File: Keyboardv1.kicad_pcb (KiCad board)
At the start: 2 copper layers, 168 parts, among them SW1 SW_Push_45deg, SW10 SW_Push_45deg, SW11 SW_Push_45deg, SW12 SW_Push_45deg, SW13 SW_Push_45deg, SW14 SW_Push_45deg, SW15 SW_Push_45deg, SW16 SW_Push_45deg, SW17 SW_Push_45deg, SW18 SW_Push_45deg, SW19 SW_Push_45deg, SW2 SW_Push_45deg, SW20 SW_Push_45deg, SW21 SW_Push_45deg, SW22 SW_Push_45deg, SW23 SW_Push_45deg, SW24 SW_Push_45deg, SW25 SW_Push_45deg, SW26 SW_Push_45deg, SW27 SW_Push_45deg, SW28 SW_Push_45deg, SW29 SW_Push_45deg, SW3 SW_Push_45deg, SW30 SW_Push_45deg, SW31 SW_Push_45deg, SW32 SW_Push_45deg, SW33 SW_Push_45deg, SW34 SW_Push_45deg, SW35 SW_Push_45deg, SW36 SW_Push_45deg, SW37 SW_Push_45deg, SW38 SW_Push_45deg, SW39 SW_Push_45deg, SW4 SW_Push_45deg, SW40 SW_Push_45deg, SW41 SW_Push_45deg, SW42 SW_Push_45deg, SW43 SW_Push_45deg, SW44 SW_Push_45deg, SW45 SW_Push_45deg, SW46 SW_Push_45deg, SW47 SW_Push_45deg, SW48 SW_Push_45deg, SW49 SW_Push_45deg, SW5 SW_Push_45deg, SW50 SW_Push_45deg, SW51 SW_Push_45deg, SW52 SW_Push_45deg, SW53 SW_Push_45deg, SW54 SW_Push_45deg, SW55 SW_Push_45deg, SW56 SW_Push_45deg, SW57 SW_Push_45deg, SW58 SW_Push_45deg, SW59 SW_Push_45deg, SW6 SW_Push_45deg, SW60 SW_Push_45deg, SW61 SW_Push_45deg, SW62 SW_Push_45deg, SW63 SW_Push_45deg, SW64 SW_Push_45deg, SW65 SW_Push_45deg, SW66 SW_Push_45deg, SW67 SW_Push_45deg, SW68 SW_Push_45deg, SW69 SW_Push_45deg, SW7 SW_Push_45deg, SW70 SW_Push_45deg, SW71 SW_Push_45deg, SW72 SW_Push_45deg, SW73 SW_Push_45deg, SW74 SW_Push_45deg, SW75 SW_Push_45deg, SW76 SW_Push_45deg, SW77 SW_Push_45deg, SW78 SW_Push_45deg, SW79 SW_Push_45deg, SW8 SW_Push_45deg, SW80 SW_Push_45deg, SW81 SW_Push_45deg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

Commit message: update
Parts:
- added U1: ESP32-S3-WROOM-1, PCM_Espressif:ESP32-S3-WROOM-1, F.Cu at (237.9, 167.4)
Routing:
- net row1: track 571.5 -> 285.8 mm
- net row0: track 571.5 -> 285.8 mm
- net col12: track 275.9 -> 92.0 mm
- net col2: track 220.1 -> 110.0 mm
- net col0: track 208.3 -> 104.1 mm
- net col11: track 178.0 -> 89.0 mm
- net col8: track 172.1 -> 86.1 mm
- net col6: track 172.1 -> 86.1 mm
- net col5: track 172.1 -> 86.1 mm
- net col3: track 172.1 -> 86.1 mm
- net col1: track 172.1 -> 86.1 mm
- net col4: track 172.1 -> 86.1 mm
- net col7: track 172.1 -> 86.1 mm
- net col10: track 172.1 -> 86.1 mm
- net col9: track 172.1 -> 86.1 mm
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
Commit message: update
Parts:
- added C1: 0.1u, Capacitor_SMD:C_0805_2012Metric_Pad1.18x1.45mm_HandSolder, F.Cu at (288.0, 30.1)
- added C2: C, Capacitor_SMD:C_0805_2012Metric_Pad1.18x1.45mm_HandSolder, F.Cu at (288.0, 33.1)
- added D85: LED, LED_SMD:LED_0805_2012Metric_Pad1.15x1.40mm_HandSolder, F.Cu at (285.9, 40.1)
- added D86: LED, LED_SMD:LED_0805_2012Metric_Pad1.15x1.40mm_HandSolder, F.Cu at (285.9, 43.1)
- added P1: USB_C_Plug_USB2.0, Connector_USB:USB_C_Receptacle_GCT_USB4105-xx-A_16P_TopMnt_Horizontal, F.Cu at (312.3, 40.1)
- added Q1: FS8205A, FS8205A:SOP65P640X120-8N, F.Cu at (290.0, 47.9)
- added R1: 100, Resistor_SMD:R_0805_2012Metric_Pad1.20x1.40mm_HandSolder, F.Cu at (271.5, 30.0)
- added R2: 1K, Resistor_SMD:R_0805_2012Metric_Pad1.20x1.40mm_HandSolder, F.Cu at (271.5, 33.0)
- added R3: 1k, Resistor_SMD:R_0805_2012Metric_Pad1.20x1.40mm_HandSolder, F.Cu at (271.5, 35.9)
- added R4: 1k, Resistor_SMD:R_0805_2012Metric_Pad1.20x1.40mm_HandSolder, F.Cu at (271.5, 38.9)
- added R5: R, Resistor_SMD:R_0805_2012Metric_Pad1.20x1.40mm_HandSolder, F.Cu at (271.5, 41.8)
- added U2: TP4056-42-ESOP8, Package_SO:SOIC-8-1EP_3.9x4.9mm_P1.27mm_EP2.41x3.3mm_ThermalVias, F.Cu at (298.8, 52.7)
- added U3: DW01A, Package_TO_SOT_SMD:SOT-23-6, F.Cu at (287.8, 55.1)
- moved U1 160.0 mm to (343.5, 47.2), turned to -90 degrees
- moved D28 43.1 mm to (280.8, 92.9)
- moved SW27 43.1 mm to (256.7, 89.9)
- moved SW71 43.1 mm to (280.5, 147.1)
- moved D20 43.1 mm to (128.4, 92.9)
- moved D56 43.1 mm to (257.0, 131.0)
- moved D64 43.1 mm to (152.2, 150.1)
- moved D80 43.1 mm to (280.8, 169.1)
- moved SW21 43.1 mm to (142.4, 89.9)
- moved SW79 43.1 mm to (256.7, 166.1)
- moved D12 43.1 mm to (280.8, 73.9)
- moved D17 43.1 mm to (71.2, 92.9)
- moved D18 43.1 mm to (90.3, 92.9)
- moved D61 43.1 mm to (83.1, 150.1)
- moved SW11 43.1 mm to (256.7, 70.8)
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
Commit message: almost done
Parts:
- added C3: 22u, Capacitor_SMD:C_0805_2012Metric_Pad1.18x1.45mm_HandSolder, F.Cu at (191.1, 50.6)
- added C4: 0.1u, Capacitor_SMD:C_0805_2012Metric_Pad1.18x1.45mm_HandSolder, F.Cu at (188.1, 50.6)
- added C5: 1u, Capacitor_SMD:C_0805_2012Metric_Pad1.18x1.45mm_HandSolder, F.Cu at (193.0, 55.1)
- added C8: 0.1u, Capacitor_SMD:C_0805_2012Metric_Pad1.18x1.45mm_HandSolder, F.Cu at (187.9, 57.9)
- added D87: LED, LED_SMD:LED_0805_2012Metric_Pad1.15x1.40mm_HandSolder, F.Cu at (181.2, 46.4)
- added J1: Conn_01x02_Pin, Connector_PinHeader_2.54mm:PinHeader_1x02_P2.54mm_Vertical, F.Cu at (171.3, 57.7)
- added J2: Conn_01x02_Pin, Connector_PinHeader_2.54mm:PinHeader_1x02_P2.54mm_Vertical, F.Cu at (165.4, 70.0)
- added J3: Conn_01x02_Pin, Connector_JST:JST_PH_B2B-PH-K_1x02_P2.00mm_Vertical, F.Cu at (162.5, 60.0)
- added J4: Conn_01x09_Pin, Connector_PinHeader_2.54mm:PinHeader_1x09_P2.54mm_Vertical, F.Cu at (222.2, 67.5)
- added J5: Conn_01x02_Pin, Connector_PinHeader_2.54mm:PinHeader_1x02_P2.54mm_Vertical, F.Cu at (226.4, 54.8)
- added J6: Conn_01x02_Pin, Connector_PinHeader_2.54mm:PinHeader_1x02_P2.54mm_Vertical, F.Cu at (180.1, 51.2)
- added R10: 10k, Resistor_SMD:R_0805_2012Metric_Pad1.20x1.40mm_HandSolder, B.Cu at (306.9, 88.2)
- added R11: 10k, Resistor_SMD:R_0805_2012Metric_Pad1.20x1.40mm_HandSolder, B.Cu at (307.4, 107.2)
- added R12: 10k, Resistor_SMD:R_0805_2012Metric_Pad1.20x1.40mm_HandSolder, B.Cu at (297.2, 126.2)
- added R13: 10k, Resistor_SMD:R_0805_2012Metric_Pad1.20x1.40mm_HandSolder, B.Cu at (303.4, 145.5)
- added R14: 10k, Resistor_SMD:R_0805_2012Metric_Pad1.20x1.40mm_HandSolder, B.Cu at (345.2, 164.5)
- added R15: 10k, Resistor_SMD:R_0805_2012Metric_Pad1.20x1.40mm_HandSolder, B.Cu at (344.9, 88.0)
- added R6: 10k, Resistor_SMD:R_0805_2012Metric_Pad1.20x1.40mm_HandSolder, F.Cu at (194.1, 50.6)
- added R7: 1k, Resistor_SMD:R_0805_2012Metric_Pad1.20x1.40mm_HandSolder, F.Cu at (185.6, 46.4)
- added R8: 10k, Resistor_SMD:R_0805_2012Metric_Pad1.20x1.40mm_HandSolder, F.Cu at (234.5, 71.5)
- added R9: 10k, Resistor_SMD:R_0805_2012Metric_Pad1.20x1.40mm_HandSolder, F.Cu at (234.5, 64.0)
- added REF**: MountingHole_3.2mm_M3, MountingHole:MountingHole_3.2mm_M3, F.Cu at (322.0, 159.0)
- added REF**: MountingHole_3.2mm_M3, MountingHole:MountingHole_3.2mm_M3, F.Cu at (100.0, 159.0)
- added REF**: Stabilizer_Cherry_MX_6.25u, PCM_Mounting_Keyboard_Stabilizer:Stabilizer_Cherry_MX_6.25u, F.Cu at (190.2, 178.8)
- added REF**: MountingHole_3.2mm_M3, MountingHole:MountingHole_3.2mm_M3, F.Cu at (307.0, 94.0)
- added REF**: Stabilizer_Cherry_MX_2.00u, PCM_Mounting_Keyboard_Stabilizer:Stabilizer_Cherry_MX_2.00u, F.Cu at (323.5, 140.8)
- added REF**: MountingHole_3.2mm_M3, MountingHole:MountingHole_3.2mm_M3, F.Cu at (188.0, 150.0)
- added REF**: MountingHole_3.2mm_M3, MountingHole:MountingHole_3.2mm_M3, F.Cu at (66.0, 50.0)
- added REF**: MountingHole_3.2mm_M3, MountingHole:MountingHole_3.2mm_M3, F.Cu at (204.0, 180.0)
- added REF**: MountingHole_3.2mm_M3, MountingHole:MountingHole_3.2mm_M3, F.Cu at (97.0, 93.0)
- added REF**: MountingHole_3.2mm_M3, MountingHole:MountingHole_3.2mm_M3, F.Cu at (240.0, 50.0)
- added REF**: MountingHole_3.2mm_M3, MountingHole:MountingHole_3.2mm_M3, F.Cu at (315.0, 50.0)
- added REF**: MountingHole_3.2mm_M3, MountingHole:MountingHole_3.2mm_M3, F.Cu at (173.5, 93.0)
- added REF**: MountingHole_3.2mm_M3, MountingHole:MountingHole_3.2mm_M3, F.Cu at (358.0, 50.0)
- added REF**: MountingHole_3.2mm_M3, MountingHole:MountingHole_3.2mm_M3, F.Cu at (265.0, 50.0)
- added REF**: MountingHole_3.2mm_M3, MountingHole:MountingHole_3.2mm_M3, F.Cu at (290.0, 50.0)
- added REF**: Stabilizer_Cherry_MX_2.00u, PCM_Mounting_Keyboard_Stabilizer:Stabilizer_Cherry_MX_2.00u, F.Cu at (325.9, 102.7)
- added REF**: Stabilizer_Cherry_MX_2.00u, PCM_Mounting_Keyboard_Stabilizer:Stabilizer_Cherry_MX_2.00u, F.Cu at (80.6, 159.8)
- added SW85: SW_Push, Button_Switch_THT:SW_PUSH_6mm, F.Cu at (183.9, 60.3)
- added SW86: SW_Push, Button_Switch_THT:SW_PUSH_6mm, F.Cu at (177.4, 70.0)
- added SW87: SW_Push, Button_Switch_THT:SW_PUSH_6mm, F.Cu at (238.0, 59.0)
- added SW88: SW_SPDT, Button_Switch_THT:SW_Slide_SPDT_Angled_CK_OS102011MA1Q, F.Cu at (151.9, 47.0)
- added SW89: SW_Push, Button_Switch_THT:SW_PUSH_6mm, F.Cu at (238.0, 67.5)
- added TP1: TestPoint, TestPoint:TestPoint_Pad_D1.0mm, B.Cu at (78.2, 91.0)
- added TP10: TestPoint, TestPoint:TestPoint_Pad_D1.0mm, F.Cu at (127.8, 74.2)
- added TP11: TestPoint, TestPoint:TestPoint_Pad_D1.0mm, F.Cu at (146.2, 74.5)
- added TP12: TestPoint, TestPoint:TestPoint_Pad_D1.0mm, F.Cu at (164.8, 75.0)
- added TP13: TestPoint, TestPoint:TestPoint_Pad_D1.0mm, F.Cu at (188.0, 68.8)
- added TP14: TestPoint, TestPoint:TestPoint_Pad_D1.0mm, F.Cu at (193.8, 68.8)
- added TP15: TestPoint, TestPoint:TestPoint_Pad_D1.0mm, F.Cu at (198.5, 72.8)
- added TP16: TestPoint, TestPoint:TestPoint_Pad_D1.0mm, F.Cu at (230.5, 77.5)
- added TP17: TestPoint, TestPoint:TestPoint_Pad_D1.0mm, F.Cu at (249.8, 77.2)
- added TP18: TestPoint, TestPoint:TestPoint_Pad_D1.0mm, F.Cu at (268.8, 76.6)
- added TP19: TestPoint, TestPoint:TestPoint_Pad_D1.0mm, F.Cu at (288.8, 75.2)
- added TP2: TestPoint, TestPoint:TestPoint_Pad_D1.0mm, B.Cu at (78.2, 110.2)
- added TP20: TestPoint, TestPoint:TestPoint_Pad_D1.0mm, F.Cu at (307.6, 74.8)
- added TP3: TestPoint, TestPoint:TestPoint_Pad_D1.0mm, B.Cu at (85.5, 129.2)
- added TP4: TestPoint, TestPoint:TestPoint_Pad_D1.0mm, B.Cu at (89.0, 144.8)
- added TP5: TestPoint, TestPoint:TestPoint_Pad_D1.0mm, B.Cu at (99.8, 166.5)
- added TP6: TestPoint, TestPoint:TestPoint_Pad_D1.0mm, B.Cu at (83.5, 182.8)
- added TP7: TestPoint, TestPoint:TestPoint_Pad_D1.0mm, F.Cu at (74.8, 71.2)
- added TP8: TestPoint, TestPoint:TestPoint_Pad_D1.0mm, F.Cu at (90.0, 73.5)
- added TP9: TestPoint, TestPoint:TestPoint_Pad_D1.0mm, F.Cu at (109.0, 73.8)
- added U4: MCP1700x-330xxTT, Package_TO_SOT_SMD:SOT-23W_Handsoldering, F.Cu at (160.0, 46.9)
- C2: value C -> 0.1u
- moved U2 157.0 mm to (142.0, 61.4)
- moved C2 152.4 mm to (137.9, 60.1), turned to 90 degrees
- moved C1 143.5 mm to (147.1, 57.0), turned to -90 degrees
- moved P1 141.5 mm to (171.0, 47.5)
- moved D86 141.5 mm to (147.1, 70.9)
- moved D85 141.3 mm to (147.1, 67.2)
- moved Q1 139.6 mm to (151.5, 65.9)
- moved U1 136.5 mm to (207.6, 59.6), turned to 0 degrees
- moved U3 136.0 mm to (151.8, 58.5), turned to 90 degrees
- moved R3 134.2 mm to (141.9, 70.9)
- moved R4 132.6 mm to (141.9, 67.2)
- moved R5 128.7 mm to (143.5, 55.6)
- moved R1 123.9 mm to (149.8, 53.3)
- moved R2 118.8 mm to (156.0, 60.8), turned to -90 degrees
- moved D13 13.8 mm to (301.3, 87.6)
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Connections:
- net /Power/B- renamed -BATT
- C2 pad 1: P- -> GND
- D15 pad 1: row0 -> row5
- D16 pad 1: row0 -> row5
- D31 pad 1: row1 -> row5
- D46 pad 1: row2 -> row5
- P1 pad A1: P- -> GND
- P1 pad A12: P- -> GND
- P1 pad A6: unconnected-(P1-D+-PadA6) -> USB_D+
- P1 pad A7: unconnected-(P1-D--PadA7) -> USB_D-
- P1 pad B1: P- -> GND
- P1 pad B12: P- -> GND
- Q1 pad 6: P- -> GND
- Q1 pad 7: P- -> GND
- R1 pad 1: P+ -> +BATT
- R2 pad 2: P- -> GND
- R5 pad 2: P- -> GND
- SW15 pad 1: col14 -> col10
- SW16 pad 1: col15 -> col13
- SW31 pad 1: col14 -> col11
- SW46 pad 1: col14 -> col12
- U1 pad 1: Net-(U1-GND-Pad1) -> GND
- U1 pad 10: unconnected-(U1-GPIO17/U1TXD/ADC2_CH6-Pad10) -> col6
- U1 pad 11: unconnected-(U1-GPIO18/U1RXD/ADC2_CH7/CLK_OUT3-Pad11) -> col7
- U1 pad 12: unconnected-(U1-GPIO8/TOUCH8/ADC1_CH7/SUBSPICS1-Pad12) -> col8
- U1 pad 13: unconnected-(U1-GPIO19/U1RTS/ADC2_CH8/CLK_OUT2/USB_D--Pad13) -> USB_D-
- U1 pad 14: unconnected-(U1-GPIO20/U1CTS/ADC2_CH9/CLK_OUT1/USB_D+-Pad14) -> USB_D+
- U1 pad 15: unconnected-(U1-GPIO3/TOUCH3/ADC1_CH2-Pad15) -> col9
- U1 pad 16: unconnected-(U1-GPIO46-Pad16) -> col10
- U1 pad 17: unconnected-(U1-GPIO9/TOUCH9/ADC1_CH8/FSPIHD/SUBSPIHD-Pad17) -> col11
- U1 pad 18: unconnected-(U1-GPIO10/TOUCH10/ADC1_CH9/FSPICS0/FSPIIO4/SUBSPICS0-Pad18) -> col12
- U1 pad 19: unconnected-(U1-GPIO11/TOUCH11/ADC2_CH0/FSPID/FSPIIO5/SUBSPID-Pad19) -> col13
- U1 pad 2: unconnected-(U1-3V3-Pad2) -> +3.3V
- U1 pad 20: unconnected-(U1-GPIO12/TOUCH12/ADC2_CH1/FSPICLK/FSPIIO6/SUBSPICLK-Pad20) -> row0
- U1 pad 21: unconnected-(U1-GPIO13/TOUCH13/ADC2_CH2/FSPIQ/FSPIIO7/SUBSPIQ-Pad21) -> row1
- U1 pad 22: unconnected-(U1-GPIO14/TOUCH14/ADC2_CH3/FSPIWP/FSPIDQS/SUBSPIWP-Pad22) -> row2
- U1 pad 23: unconnected-(U1-GPIO21-Pad23) -> row3
- U1 pad 24: unconnected-(U1-GPIO47/SPICLK_P/SUBSPICLK_P_DIFF-Pad24) -> Net-(J4-Pin_9)
- U1 pad 25: unconnected-(U1-GPIO48/SPICLK_N/SUBSPICLK_N_DIFF-Pad25) -> Net-(J4-Pin_8)
- U1 pad 26: unconnected-(U1-GPIO45-Pad26) -> row4
- U1 pad 27: unconnected-(U1-GPIO0/BOOT-Pad27) -> /MCU/BOOT
- U1 pad 28: unconnected-(U1-SPIIO6/GPIO35/FSPID/SUBSPID-Pad28) -> Net-(J4-Pin_5)
- U1 pad 29: unconnected-(U1-SPIIO7/GPIO36/FSPICLK/SUBSPICLK-Pad29) -> Net-(J4-Pin_6)
- U1 pad 3: unconnected-(U1-EN-Pad3) -> Net-(J1-Pin_1)
- U1 pad 30: unconnected-(U1-SPIDQS/GPIO37/FSPIQ/SUBSPIQ-Pad30) -> Net-(J4-Pin_7)
- U1 pad 31: unconnected-(U1-GPIO38/FSPIWP/SUBSPIWP-Pad31) -> row5
- U1 pad 32: unconnected-(U1-MTCK/GPIO39/CLK_OUT3/SUBSPICS1-Pad32) -> Net-(J4-Pin_1)
- U1 pad 33: unconnected-(U1-MTDO/GPIO40/CLK_OUT2-Pad33) -> Net-(J4-Pin_2)
- U1 pad 34: unconnected-(U1-MTDI/GPIO41/CLK_OUT1-Pad34) -> Net-(J4-Pin_3)
- U1 pad 35: unconnected-(U1-MTMS/GPIO42-Pad35) -> Net-(J4-Pin_4)
- U1 pad 38: unconnected-(U1-GPIO2/TOUCH2/ADC1_CH1-Pad38) -> Net-(J5-Pin_1)
- U1 pad 39: unconnected-(U1-GPIO1/TOUCH1/ADC1_CH0-Pad39) -> Net-(J5-Pin_2)
- U1 pad 4: unconnected-(U1-GPIO4/TOUCH4/ADC1_CH3-Pad4) -> col0
- U1 pad 40: Net-(U1-GND-Pad1) -> GND
- U1 pad 41: Net-(U1-GND-Pad1) -> GND
- U1 pad 5: unconnected-(U1-GPIO5/TOUCH5/ADC1_CH4-Pad5) -> col1
- U1 pad 6: unconnected-(U1-GPIO6/TOUCH6/ADC1_CH5-Pad6) -> col2
- U1 pad 7: unconnected-(U1-GPIO7/TOUCH7/ADC1_CH6-Pad7) -> col3
- U1 pad 8: unconnected-(U1-GPIO15/U0RTS/ADC2_CH4/XTAL_32K_P-Pad8) -> col4
- U1 pad 9: unconnected-(U1-GPIO16/U0CTS/ADC2_CH5/XTAL_32K_N-Pad9) -> col5
- U2 pad 1: P- -> GND
- U2 pad 3: P- -> GND
- U2 pad 5: unconnected-(U2-BAT-Pad5) -> +BATT
- U2 pad 9: P- -> GND
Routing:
- net row5: track 283.4 -> 547.1 mm, vias 0 -> 3
- net col11: track 89.0 -> 349.2 mm
- net col12: track 92.0 -> 303.4 mm, vias 0 -> 1
- net col13: track 63.1 -> 246.6 mm
- net col4: track 86.1 -> 253.2 mm
- net col1: track 86.1 -> 241.0 mm
- net col5: track 86.1 -> 235.2 mm
- net col0: track 104.1 -> 251.9 mm
- net col9: track 86.1 -> 228.5 mm
- net col10: track 86.1 -> 227.4 mm
- net col3: track 86.1 -> 222.7 mm
- net col8: track 86.1 -> 219.6 mm
- net col6: track 86.1 -> 218.9 mm
- net col7: track 86.1 -> 207.4 mm
- net +3.3V: track 0.00 -> 110.9 mm, vias 0 -> 1
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- added copper zone on B.Cu, net GND
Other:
- board outline added: 304 x 146 mm
- board text added: "3.3v GND"
- board text added: "BOOT MODE"
- board text added: "BT SELECT IO40"
- board text added: "EN_BTN"
- board text added: "GPIO1 GPIO2"
- board text added: "GPIO47 GPIO48 GPIO37 GPIO36 GPIO35 GPIO42 GPIO41 GPIO40 GPIO39"
- board text added: "OFF"
- board text added: "ON"
- board text added: "POWER CIRCUIT"
- board text added: "PWR_SW"
- board text added: "TBD IO39"
- board text added: "TP1-ROW0 TP2-ROW1 TP3-ROW2 TP4-ROW3 TP5-ROW4 TP6-ROW5"
- board text added: "TP7-COL0 TP8-COL1 TP9-COL2 TP10-COL3 TP11-COL4 TP12-COL5 TP13-COL6 TP14-COL7 TP15-COL8 TP16-COL9 TP17-COL10 TP18-COL11 TP19-COL12 TP20-COL13"

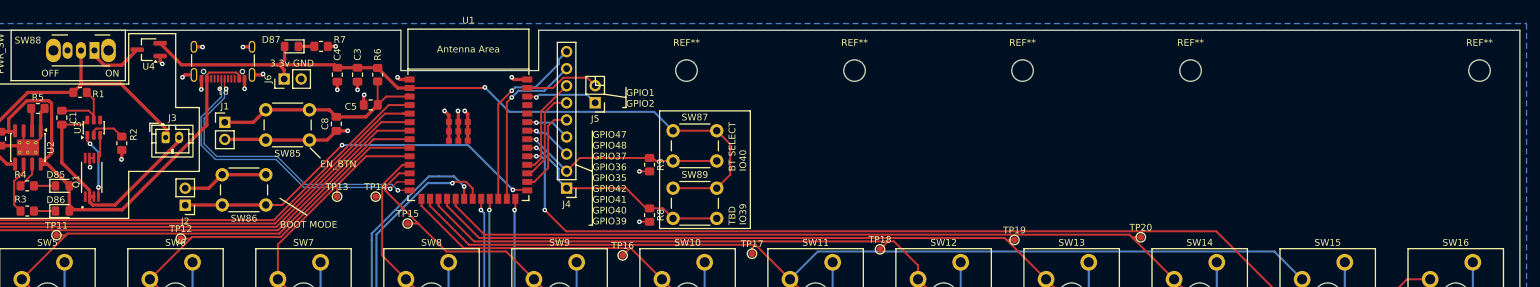
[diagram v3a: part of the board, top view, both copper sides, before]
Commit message: added more leds pins, fixed rule errors.
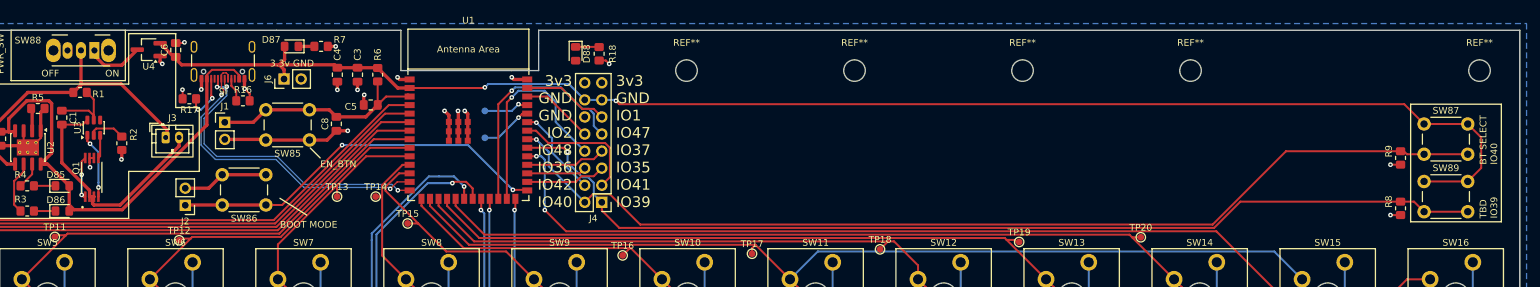
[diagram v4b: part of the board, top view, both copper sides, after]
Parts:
- removed P1: USB_C_Plug_USB2.0, Connector_USB:USB_C_Receptacle_GCT_USB4105-xx-A_16P_TopMnt_Horizontal
- added C6: 1u, Capacitor_SMD:C_0805_2012Metric_Pad1.18x1.45mm_HandSolder, F.Cu at (164.0, 46.9)
- added D88: LED, LED_SMD:LED_0805_2012Metric_Pad1.15x1.40mm_HandSolder, F.Cu at (223.5, 47.5)
- added R16: 5.1k, Resistor_SMD:R_0805_2012Metric_Pad1.20x1.40mm_HandSolder, F.Cu at (174.0, 54.5)
- added R17: 5.1k, Resistor_SMD:R_0805_2012Metric_Pad1.20x1.40mm_HandSolder, F.Cu at (166.0, 54.2)
- added R18: 1k, Resistor_SMD:R_0805_2012Metric_Pad1.20x1.40mm_HandSolder, F.Cu at (227.0, 47.5)
- added TP21: TestPoint, TestPoint:TestPoint_Pad_D1.0mm, B.Cu at (210.0, 56.0)
- added TP22: TestPoint, TestPoint:TestPoint_Pad_D1.0mm, B.Cu at (210.0, 60.0)
- J4: value Conn_01x09_Pin -> Conn_02x08_Counter_Clockwise; footprint Connector_PinHeader_2.54mm:PinHeader_1x09_P2.54mm_Vertical -> Connector_PinHeader_2.54mm:PinHeader_2x08_P2.54mm_Vertical
- J5: value Conn_01x02_Pin -> USB_C_Receptacle_USB2.0_14P; footprint Connector_PinHeader_2.54mm:PinHeader_1x02_P2.54mm_Vertical -> Connector_USB:USB_C_Receptacle_GCT_USB4105-xx-A_16P_TopMnt_Horizontal
- moved R8 111.8 mm to (346.2, 70.5)
- moved R9 111.8 mm to (346.2, 63.0)
- moved SW87 111.8 mm to (349.8, 58.0)
- moved SW89 111.8 mm to (349.8, 66.5)
- moved J5 55.9 mm to (171.0, 47.5)
- moved J4 5.64 mm to (227.4, 69.6)
- moved TP19 0.76 mm to (289.5, 75.5)
- moved TP11 0.35 mm to (146.0, 74.8)
- moved TP12 0.35 mm to (164.5, 75.2)
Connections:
- net Net-(SW88-A) renamed VCC
- Q1 pad 1: Net-(Q1-Pad1) -> unconnected-(Q1-Pad1)_1
- Q1 pad 8: Net-(Q1-Pad1) -> unconnected-(Q1-Pad1)
- U1 pad 36: unconnected-(U1-U0RXD/GPIO44/CLK_OUT2-Pad36) -> Net-(U1-U0RXD/GPIO44/CLK_OUT2)
- U1 pad 37: unconnected-(U1-U0TXD/GPIO43/CLK_OUT1-Pad37) -> Net-(U1-U0TXD/GPIO43/CLK_OUT1)
- U1 pad 38: Net-(J5-Pin_1) -> Net-(J4-Pin_10)
- U1 pad 39: Net-(J5-Pin_2) -> Net-(D88-A)
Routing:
- net Net-(J4-Pin_2): track 31.3 -> 152.4 mm
- net Net-(J4-Pin_1): track 33.6 -> 149.8 mm
- net +3.3V: track 110.9 -> 222.7 mm, vias 1 -> 2
- net Net-(D88-A): track 0.00 -> 12.9 mm
- net Net-(J4-Pin_3): track 7.30 -> 19.4 mm, vias 1 -> 0
- net Net-(J5-Pin_2): track 11.2 -> 0.00 mm
- net Net-(J4-Pin_10): track 0.00 -> 10.9 mm
- net Net-(J5-Pin_1): track 10.8 -> 0.00 mm, vias 1 -> 0
- net Net-(U1-U0RXD/GPIO44/CLK_OUT2): track 0.00 -> 7.79 mm, vias 0 -> 1
- net Net-(J5-CC2): track 0.00 -> 7.54 mm, vias 0 -> 2
- net GND: track 78.4 -> 85.3 mm, vias 17 -> 20
- net Net-(J4-Pin_4): track 6.78 -> 13.7 mm
- net Net-(J4-Pin_8): track 25.3 -> 32.1 mm
- net Net-(U1-U0TXD/GPIO43/CLK_OUT1): track 0.00 -> 6.77 mm, vias 0 -> 1
- net Net-(J4-Pin_9): track 27.9 -> 34.5 mm
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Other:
- board text added: "3v3 GND GND IO2 IO48 IO36 IO42 IO40"
- board text added: "3v3 GND IO1 IO47 IO37 IO35 IO41 IO39"
- board text removed: "GPIO1 GPIO2"
- board text removed: "GPIO47 GPIO48 GPIO37 GPIO36 GPIO35 GPIO42 GPIO41 GPIO40 GPIO39"

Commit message: udate
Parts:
- removed the REF** at (322.0, 159.0)
- removed the REF** at (100.0, 159.0)
- removed the REF** at (190.2, 178.8)
- removed the REF** at (307.0, 94.0)
- removed the REF** at (323.5, 140.8)
- removed the REF** at (188.0, 150.0)
- removed the REF** at (66.0, 50.0)
- removed the REF** at (204.0, 180.0)
- removed the REF** at (97.0, 93.0)
- removed the REF** at (240.0, 50.0)
- removed the REF** at (315.0, 50.0)
- removed the REF** at (173.5, 93.0)
- removed the REF** at (265.0, 50.0)
- removed the REF** at (290.0, 50.0)
- removed the REF** at (325.9, 102.7)
- removed the REF** at (80.6, 159.8)
- added H1: MountingHole, MountingHole:MountingHole_3.2mm_M3, F.Cu at (65.0, 49.0)
- added H10: MountingHole, MountingHole:MountingHole_3.2mm_M3, F.Cu at (269.0, 93.0)
- added H11: MountingHole, MountingHole:MountingHole_3.2mm_M3, F.Cu at (344.0, 94.5)
- added H12: MountingHole, MountingHole:MountingHole_3.2mm_M3, F.Cu at (203.0, 179.0)
- added H13: MountingHole, MountingHole:MountingHole_3.2mm_M3, F.Cu at (319.0, 122.0)
- added H14: MountingHole, MountingHole:MountingHole_3.2mm_M3, F.Cu at (322.5, 159.5)
- added H2: MountingHole, MountingHole:MountingHole_3.2mm_M3, F.Cu at (120.0, 49.0)
- added H3: MountingHole, MountingHole:MountingHole_3.2mm_M3, F.Cu at (249.0, 49.0)
- added H4: MountingHole, MountingHole:MountingHole_3.2mm_M3, F.Cu at (305.0, 49.0)
- added H5: MountingHole, MountingHole:MountingHole_3.2mm_M3, F.Cu at (97.0, 93.0)
- added H6: MountingHole, MountingHole:MountingHole_3.2mm_M3, F.Cu at (100.0, 159.0)
- added H7: MountingHole, MountingHole:MountingHole_3.2mm_M3, F.Cu at (145.0, 130.5)
- added H8: MountingHole, MountingHole:MountingHole_3.2mm_M3, F.Cu at (192.5, 93.0)
- added H9: MountingHole, MountingHole:MountingHole_3.2mm_M3, F.Cu at (226.0, 132.0)
- added ST1: ~, PCM_Mounting_Keyboard_Stabilizer:Stabilizer_Cherry_MX_2.00u, F.Cu at (80.6, 159.8)
- added ST2: ~, PCM_Mounting_Keyboard_Stabilizer:Stabilizer_Cherry_MX_2.00u, F.Cu at (325.9, 102.7)
- added ST3: ~, PCM_Mounting_Keyboard_Stabilizer:Stabilizer_Cherry_MX_2.00u, F.Cu at (323.5, 140.8)
- added ST4: ~, PCM_Mounting_Keyboard_Stabilizer:Stabilizer_Cherry_MX_6.25u, F.Cu at (190.2, 178.8)
- moved REF** 1.41 mm to (359.0, 49.0)
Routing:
- net col4: track 253.2 -> 206.4 mm
- net (no net): track 6.34 -> 0.00 mm, vias 2 -> 0
- net Net-(J4-Pin_8): track 32.1 -> 26.3 mm
- net Net-(D88-A): track 12.9 -> 17.8 mm
- net Net-(J4-Pin_9): track 34.5 -> 32.9 mm, vias 1 -> 2
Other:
- board text added: "GND 3v3 IO1 IO47 IO37 IO35 IO41 IO39"
- board text added: "GND 3v3 NA IO2 IO48 IO36 IO42 IO40"
- board text added: "Heart beat"
- board text removed: "3v3 GND GND IO2 IO48 IO36 IO42 IO40"
- board text removed: "3v3 GND IO1 IO47 IO37 IO35 IO41 IO39"

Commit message: sent to fab
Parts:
- removed J1, J2: Conn_01x02_Pin, Connector_PinHeader_2.54mm:PinHeader_1x02_P2.54mm_Vertical
- removed REF**: MountingHole_3.2mm_M3, MountingHole:MountingHole_3.2mm_M3
- added C7: 22uf, Capacitor_SMD:C_0603_1608Metric_Pad1.08x0.95mm_HandSolder, F.Cu at (161.8, 49.0)
- added H15: MountingHole, MountingHole:MountingHole_3.2mm_M3, F.Cu at (359.0, 49.0)
- added R19: 10k, Resistor_SMD:R_0805_2012Metric_Pad1.20x1.40mm_HandSolder, F.Cu at (191.0, 54.0)
- C6: value 1u -> 0.1uf; footprint Capacitor_SMD:C_0805_2012Metric_Pad1.18x1.45mm_HandSolder -> Capacitor_SMD:C_0603_1608Metric_Pad1.08x0.95mm_HandSolder
- C8: value 0.1u -> 10uf; footprint Capacitor_SMD:C_0805_2012Metric_Pad1.18x1.45mm_HandSolder -> Capacitor_SMD:C_0603_1608Metric_Pad1.08x0.95mm_HandSolder
- Q1: footprint FS8205A:SOP65P640X120-8N -> Package_TO_SOT_SMD:SOT-23-6
- R16, R17: footprint Resistor_SMD:R_0805_2012Metric_Pad1.20x1.40mm_HandSolder -> Resistor_SMD:R_0603_1608Metric_Pad0.98x0.95mm_HandSolder
- R2: value 1K -> 1k
- R5: value R -> 1.2k
- U4: value MCP1700x-330xxTT -> AP2112K-3.3; footprint Package_TO_SOT_SMD:SOT-23W_Handsoldering -> Package_TO_SOT_SMD:SOT-23-5
- moved C8 34.2 mm to (155.0, 48.8)
- moved R1 13.3 mm to (163.0, 54.0), turned to -90 degrees
- moved C1 13.1 mm to (160.0, 55.2), turned to 180 degrees
- moved Q1 11.3 mm to (162.2, 62.5), turned to 0 degrees
- moved U3 11.2 mm to (163.0, 58.2)
- moved R2 10.6 mm to (166.0, 57.2), turned to 90 degrees
- moved R6 7.62 mm to (187.0, 53.5), turned to 90 degrees
- moved D86 7.22 mm to (154.1, 69.0)
- moved R3 7.22 mm to (148.9, 69.0)
- moved C2 6.97 mm to (144.9, 59.9)
- moved R5 6.97 mm to (150.4, 55.4)
- moved D85 6.97 mm to (154.1, 66.9)
- moved R4 6.97 mm to (148.9, 66.9)
- moved U2 6.97 mm to (149.0, 61.2)
- moved C5 6.67 mm to (187.0, 58.0), turned to 90 degrees
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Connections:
- C5 pad 2: Net-(J1-Pin_1) -> Net-(U1-EN)
- C8 pad 1: GND -> Net-(SW88-A)
- C8 pad 2: Net-(J1-Pin_1) -> GND
- R6 pad 1: +3.3V -> Net-(U1-EN)
- R6 pad 2: Net-(J1-Pin_1) -> +3.3V
- SW85 pad 2: Net-(J1-Pin_1) -> Net-(U1-EN)
- SW88 pad 1: VCC -> Net-(SW88-A)
- U1 pad 3: Net-(J1-Pin_1) -> Net-(U1-EN)
- U4 pad 1: GND -> Net-(SW88-A)
- U4 pad 2: +3.3V -> GND
- U4 pad 3: VCC -> Net-(SW88-A)
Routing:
- net col4: track 206.4 -> 253.2 mm
- net Net-(J1-Pin_1): track 34.4 -> 0.00 mm
- net Net-(U1-EN): track 0.00 -> 24.7 mm
- net -BATT: track 36.2 -> 17.2 mm
- net Net-(SW88-A): track 0.00 -> 14.1 mm
- net GND: track 85.3 -> 72.3 mm, vias 20 -> 19
- net VCC: track 8.68 -> 0.00 mm
- net USB_D-: track 48.0 -> 39.8 mm
- net /Power/USB+: track 70.8 -> 63.7 mm
- net USB_D+: track 47.6 -> 41.4 mm, vias 3 -> 4
- net Net-(U3-VCC): track 10.3 -> 4.81 mm
- net Net-(U3-OD): track 9.82 -> 5.03 mm, vias 2 -> 0
- net Net-(J5-CC2): track 7.54 -> 3.49 mm, vias 2 -> 0
- net Net-(U3-CS): track 5.48 -> 3.83 mm
- net Net-(U2-~{STDBY}): track 7.97 -> 6.35 mm
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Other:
- board text added: "Keyboard V1 Matia Choi May 2 - 2026 https://www.linkedin.com/in/matiachoi/"
